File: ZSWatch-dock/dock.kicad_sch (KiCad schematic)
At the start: 23 parts, among them IC1 STM32F072CBT6, IC2 TCR3UF20A,LM_CT, IC3 TXB0104QPWRQ1, IC4 XC9265C181MR-G, J1 USB4105-GF-A, J2 8.06.16, J3 Charger and programming heade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

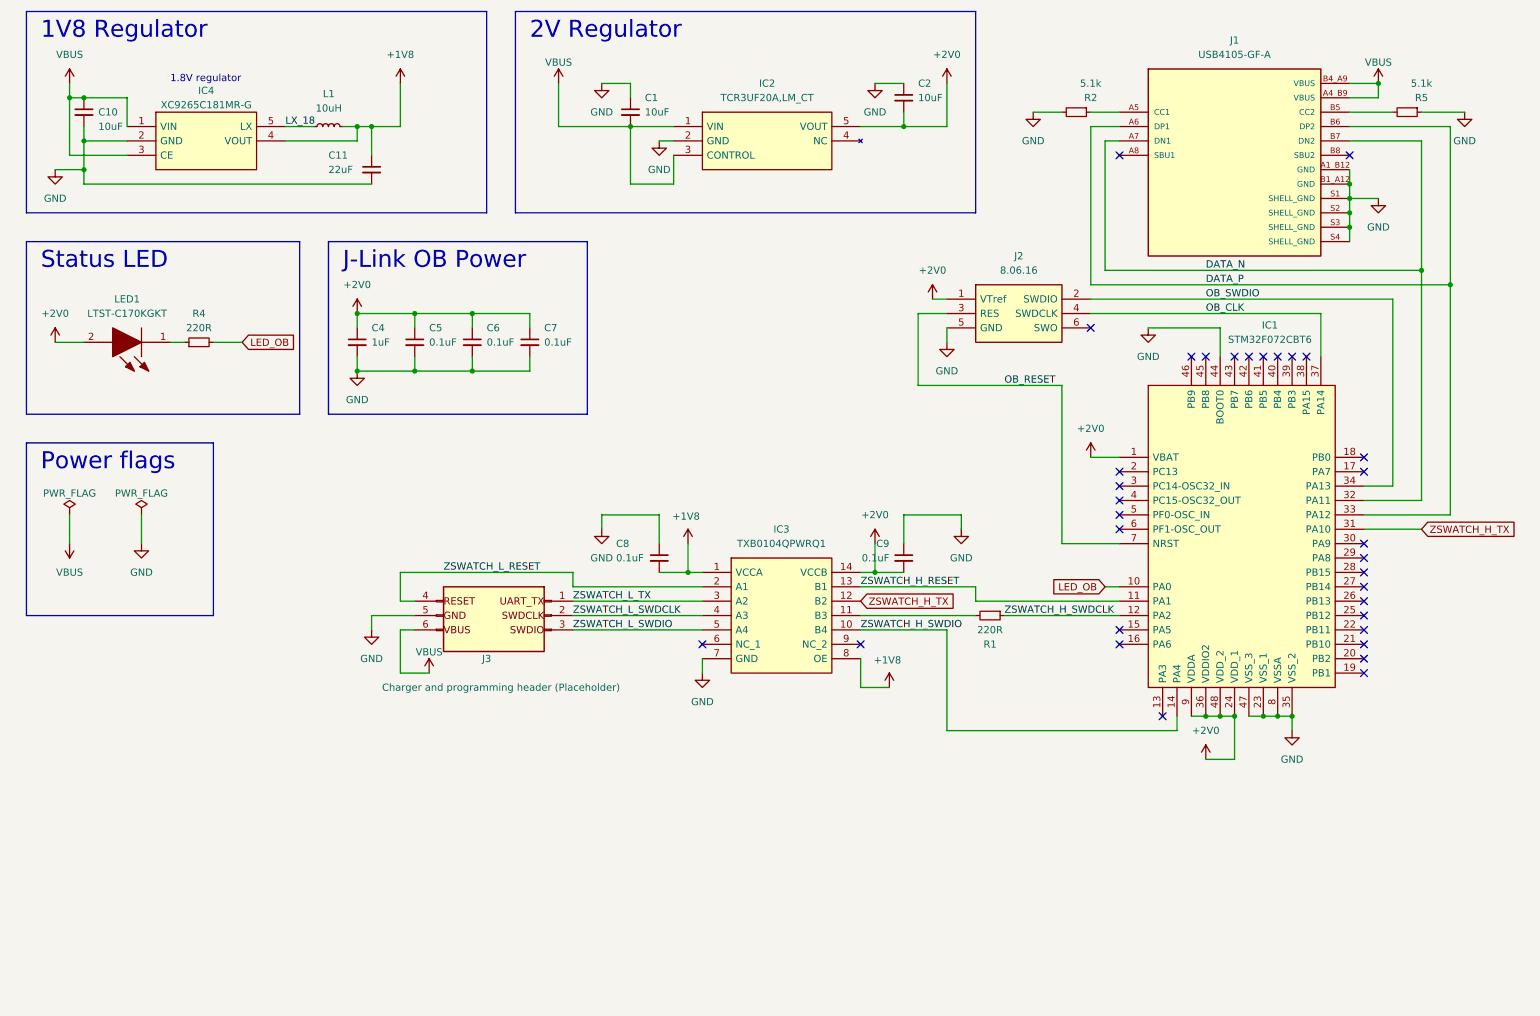
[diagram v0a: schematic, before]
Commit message: Finished dock/debugger/programmer PCB.
Moved connectors around.
Added missing silkscreen.
Added extra connector for easy access to pins such as power etc.
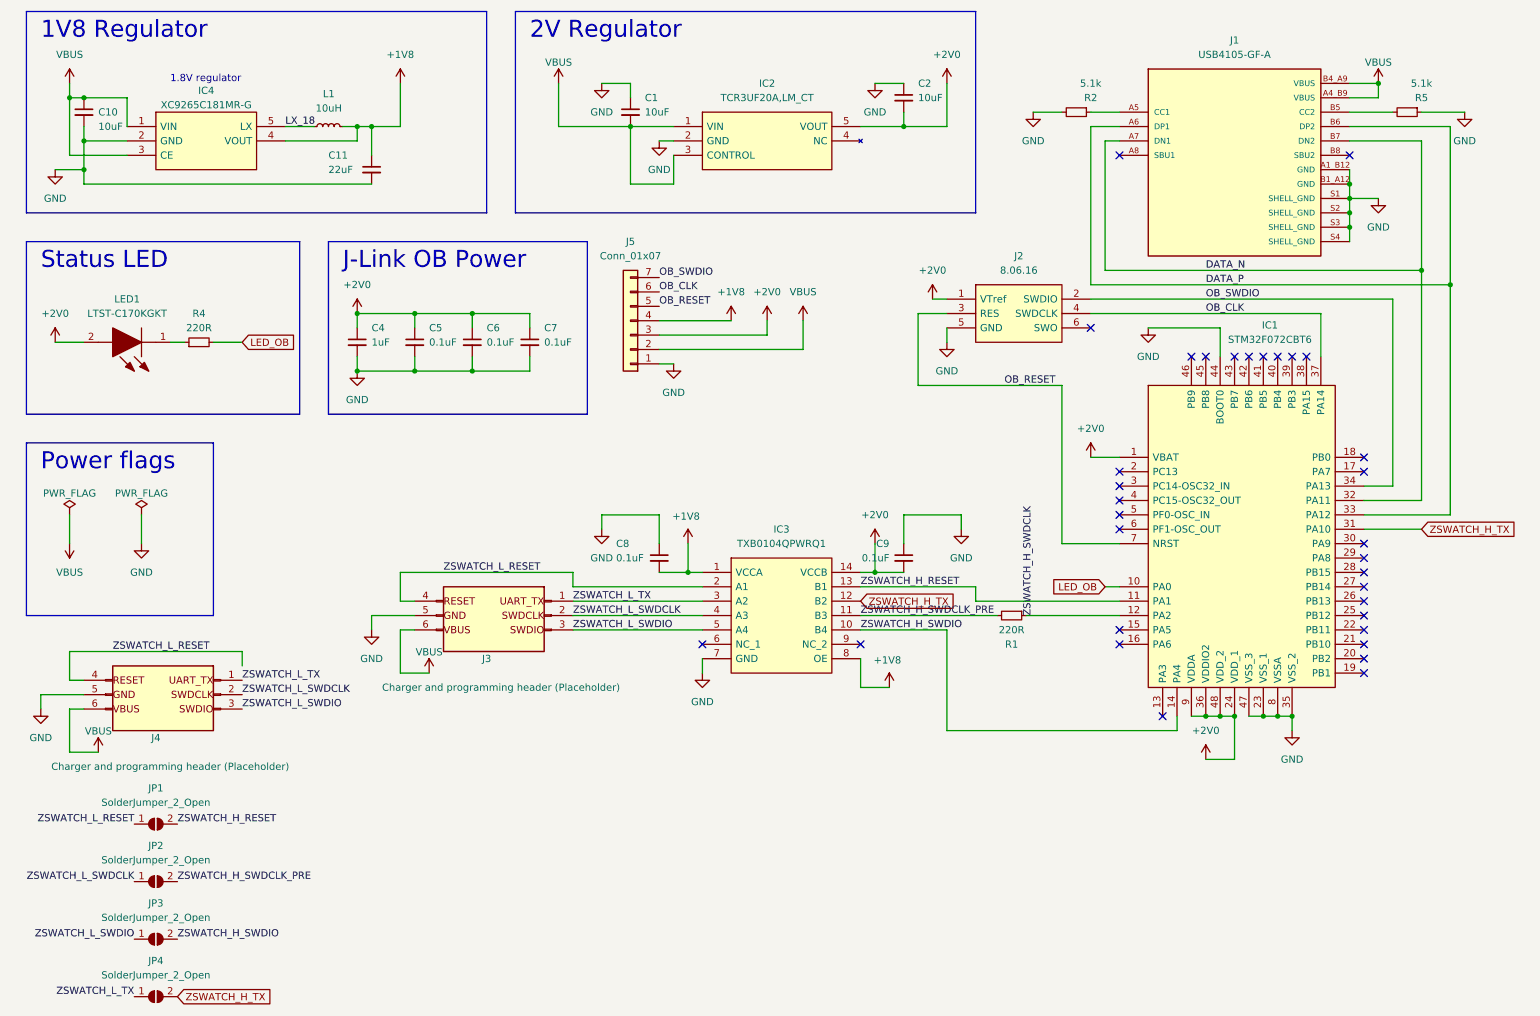
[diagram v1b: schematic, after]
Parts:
- added J4: Charger and programming header (Placeholder), user_library:rtlecs-6-pin-2-54, symbol Connector_Generic:Conn_02x04_Counter_Clockwise
- added J5: Conn_01x07, Connector_PinHeader_2.54mm:PinHeader_1x07_P2.54mm_Horizontal, symbol Connector_Generic:Conn_01x07
- added JP1, JP2, JP3, JP4: SolderJumper_2_Open, Jumper:SolderJumper-2_P1.3mm_Open_RoundedPad1.0x1.5mm, symbol Jumper:SolderJumper_2_Open
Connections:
- net +1V8: now also J5.4 (Pin_4)
- net +2V0: now also J5.3 (Pin_3)
- net GND: now also J4.5 (Pin_5), J5.1 (Pin_1)
- net OB_CLK: now also J5.6 (Pin_6)
- net OB_RESET: now also J5.5 (Pin_5)
- net OB_SWDIO: now also J5.7 (Pin_7)
- net VBUS: now also J4.6 (Pin_6), J5.2 (Pin_2)
- net ZSWATCH_H_RESET: now also JP1.2 (B)
- net ZSWATCH_H_SWDIO: now also JP3.2 (B)
- net ZSWATCH_H_TX: now also JP4.2 (B)
- net ZSWATCH_L_RESET: now also J4.4 (Pin_4), JP1.1 (A)
- net ZSWATCH_L_SWDCLK: now also J4.2 (Pin_2), JP2.1 (A)
- net ZSWATCH_L_SWDIO: now also J4.3 (Pin_3), JP3.1 (A)
- net ZSWATCH_L_TX: now also J4.1 (Pin_1), JP4.1 (A)
- net ZSWATCH_H_SWDCLK_PRE: now reaches IC3.11 (B3), R1.2
- net ZSWATCH_H_SWDCLK_PRE: now also JP2.2 (B)
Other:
- moved on the sheet: R1

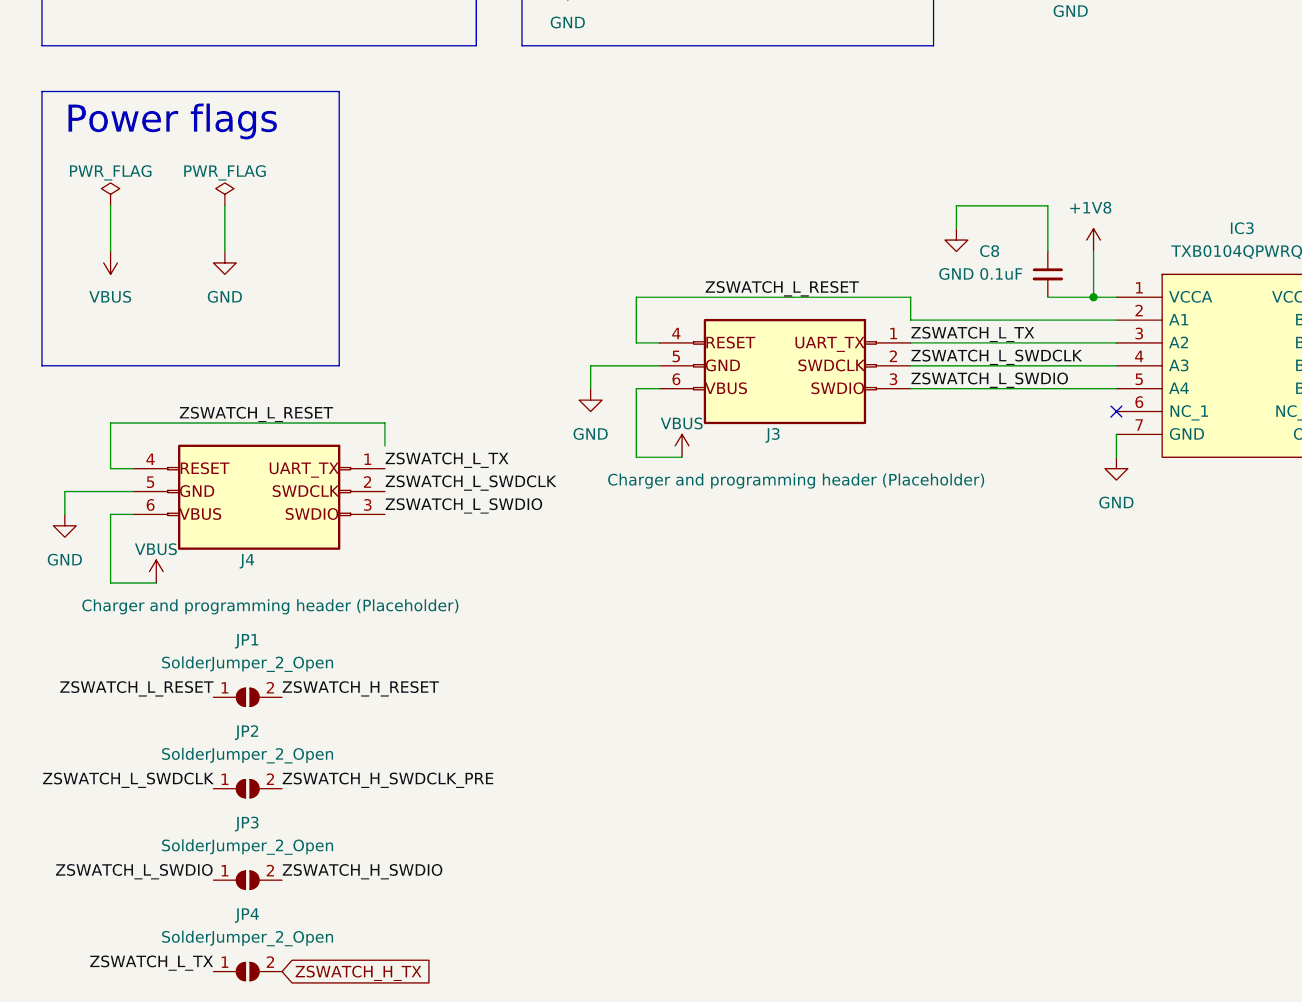
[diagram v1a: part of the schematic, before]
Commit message: Dock PCB: Minor routing and silkscreen improvements.
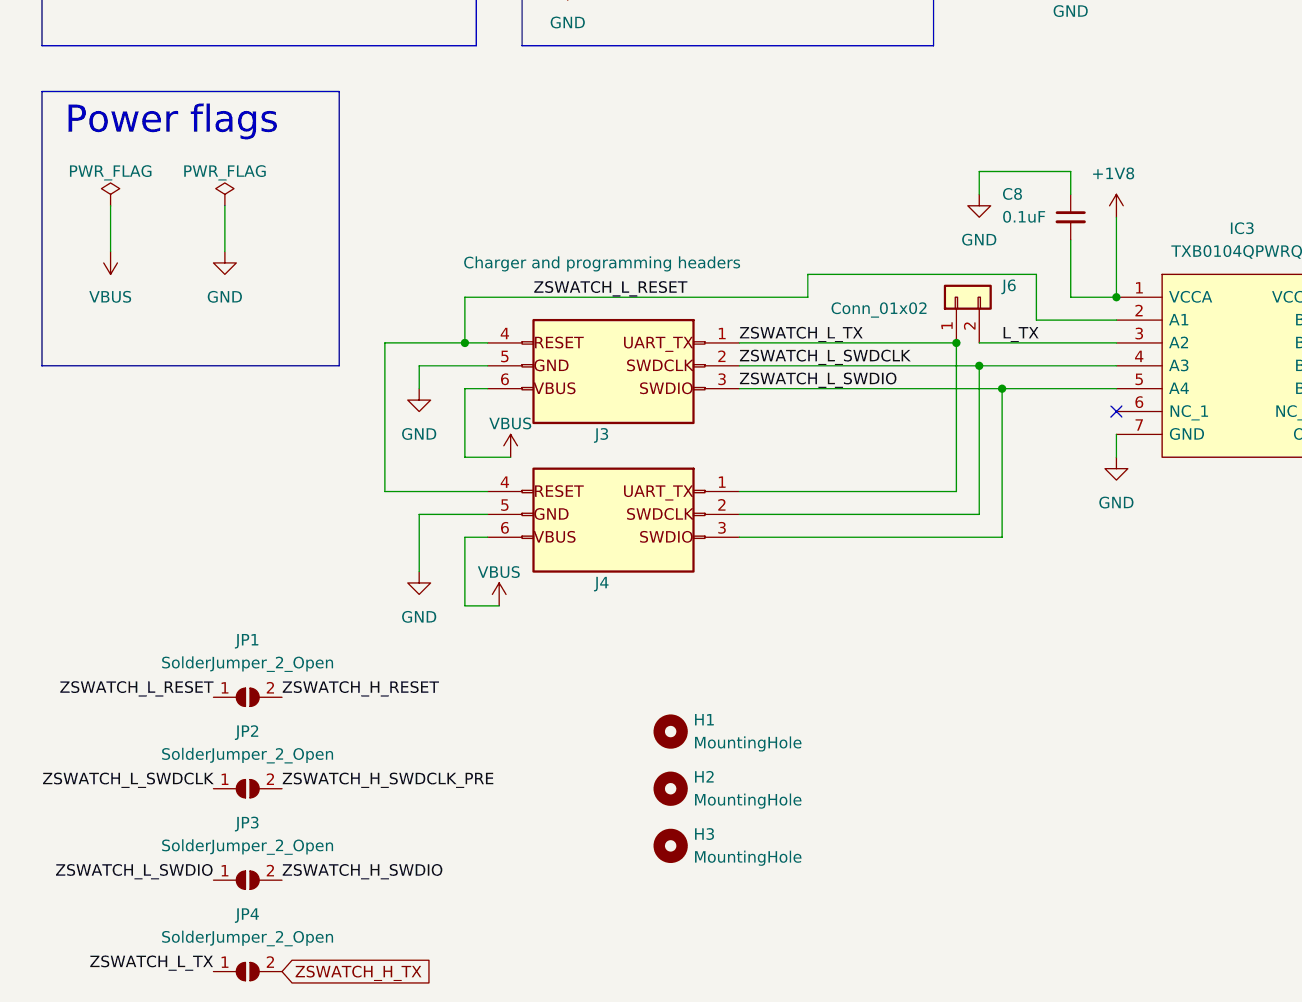
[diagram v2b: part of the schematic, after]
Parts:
- added H1, H2, H3: MountingHole, MountingHole:MountingHole_2.2mm_M2, symbol Mechanical:MountingHole
- added J6: Conn_01x02, Jumper:SolderJumper-2_P1.3mm_Bridged_Pad1.0x1.5mm, symbol Connector_Generic:Conn_01x02
- J3: value Charger and programming header (Placeholder) -> Charger and programming headers
- J4: value Charger and programming header (Placeholder) -> Charger and programming header
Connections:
- net ZSWATCH_L_TX: now also J6.1 (Pin_1); no longer IC3.3 (A2)
- new net L_TX: IC3.3 (A2), J6.2 (Pin_2)
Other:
- moved on the sheet: C8, J3, J4
